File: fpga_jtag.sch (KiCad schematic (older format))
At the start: 2 parts

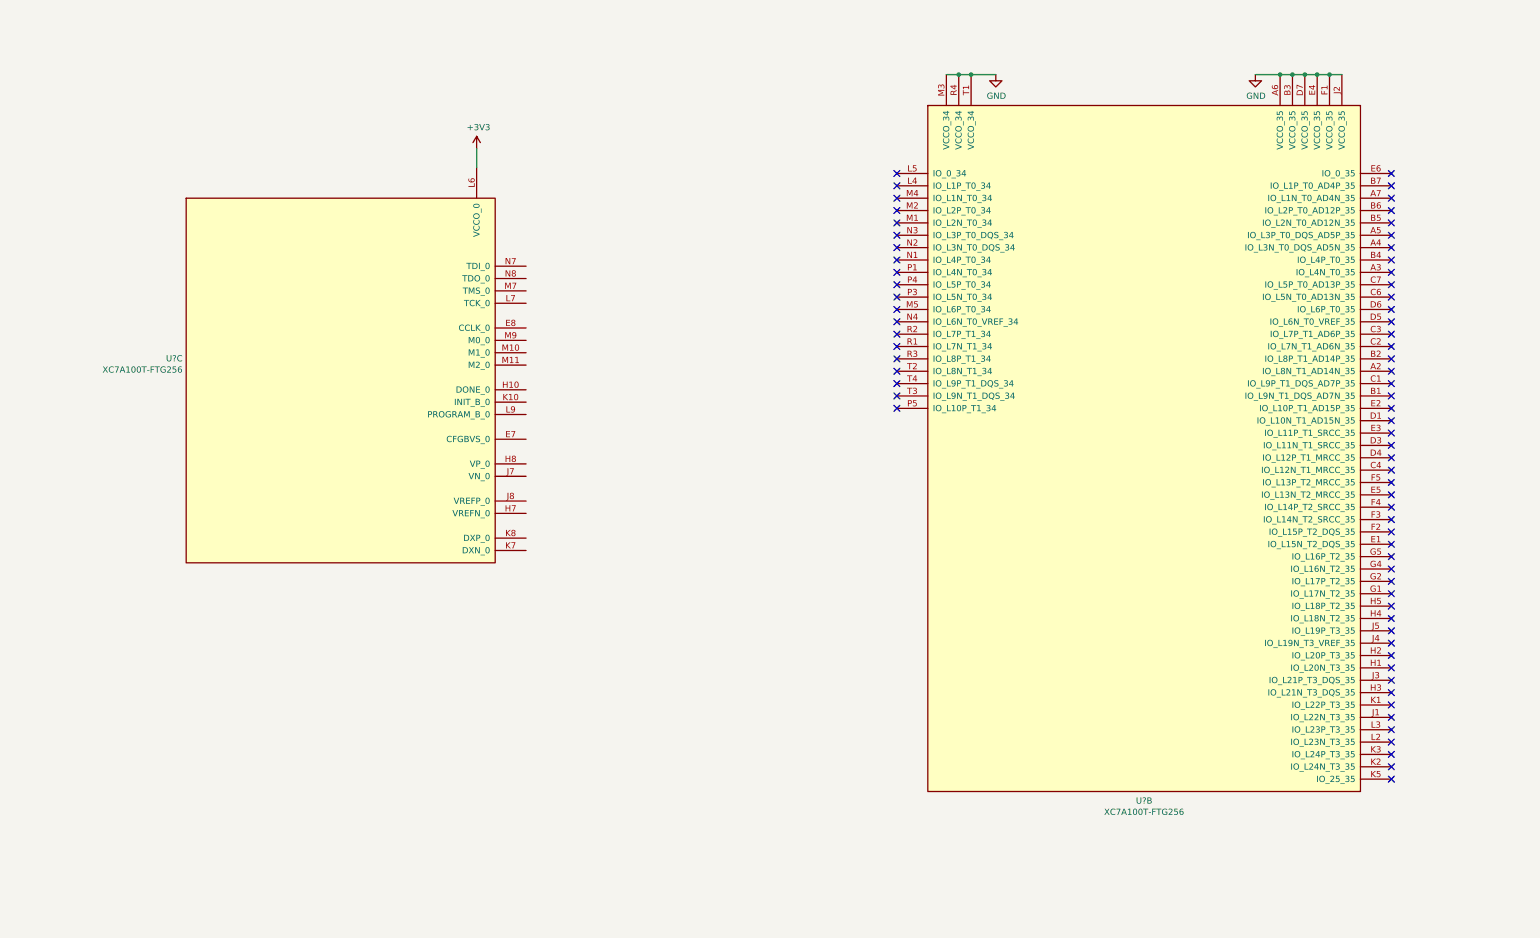
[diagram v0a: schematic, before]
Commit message: Add JTAG connector
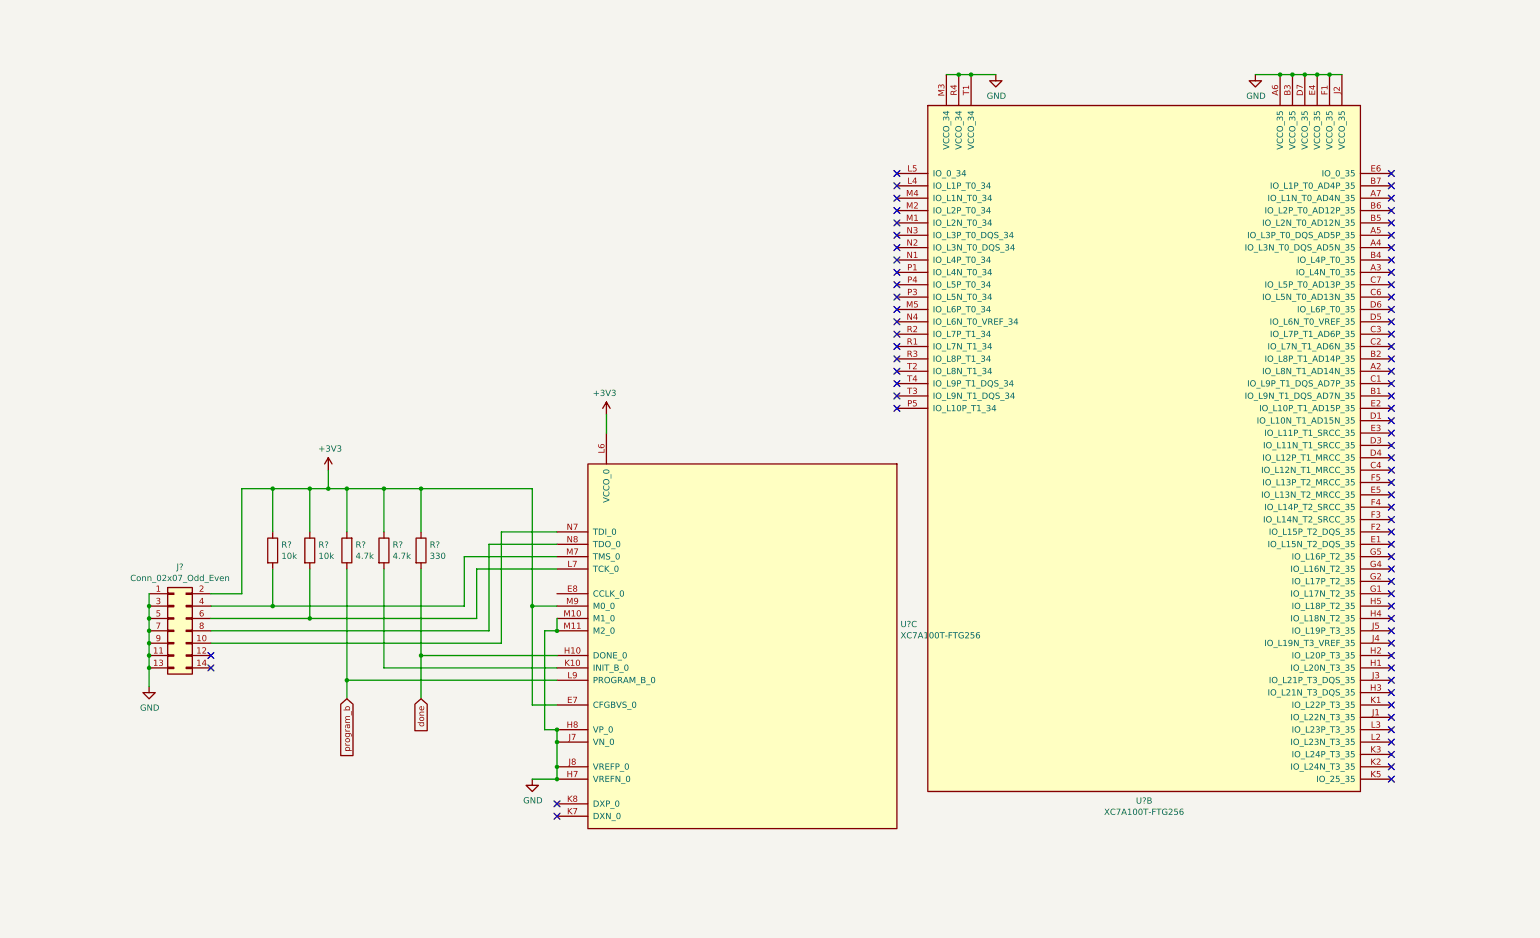
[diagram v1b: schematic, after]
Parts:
- added J?: Conn_02x07_Odd_Even, symbol Connector_Generic:Conn_02x07_Odd_Even
- added R? (x2): 10k, symbol Device:R
- added R? (x2): 4.7k, symbol Device:R
- added R?: 330, symbol Device:R
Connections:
- net +3V3: now also U?.E7 (CFGBVS_0), U?.M9 (M0_0), J?.2 (Pin_2), R?.1, R?.1, R?.1, R?.1, R?.2
- net GND: now also U?.H7 (VREFN_0), U?.H8 (VP_0), U?.J7 (VN_0), U?.J8 (VREFP_0), U?.M10 (M1_0), U?.M11 (M2_0), J?.1 (Pin_1), J?.11 (Pin_11), J?.13 (Pin_13), J?.3 (Pin_3), J?.5 (Pin_5), J?.7 (Pin_7), J?.9 (Pin_9)
- net done: now reaches U?.H10 (DONE_0)
- net done: now also R?.2
- net at U?.K10 (INIT_B_0): now also R?.2
- net at U?.L7 (TCK_0): now also J?.6 (Pin_6), R?.2
- net program_b: now reaches U?.L9 (PROGRAM_B_0)
- net program_b: now also R?.1
- net at U?.M7 (TMS_0): now also J?.4 (Pin_4), R?.2
- net at U?.N7 (TDI_0): now also J?.10 (Pin_10)
- net at U?.N8 (TDO_0): now also J?.8 (Pin_8)
- no-connect marks 70 -> 74
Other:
- moved on the sheet: U?C

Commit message: Switch FPGA I/O banks, and add subsheet for SRAM
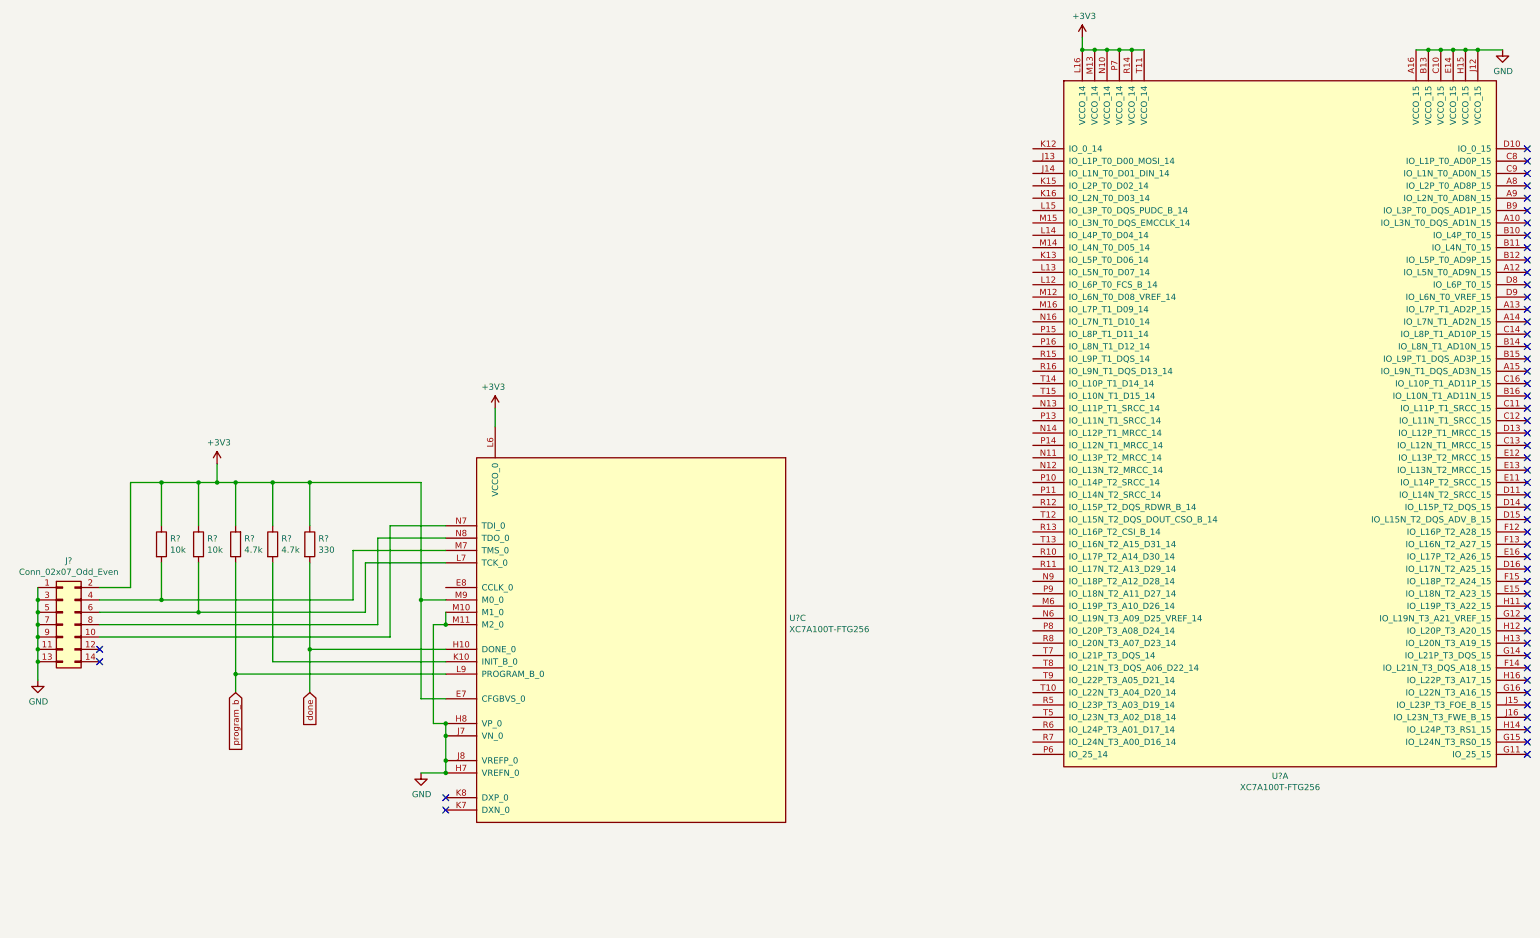
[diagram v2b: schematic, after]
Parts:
- removed U?: XC7A100T-FTG256, symbol FPGA_Xilinx_Artix7:XC7A100T-FTG256
- added U?: XC7A100T-FTG256, symbol FPGA_Xilinx_Artix7:XC7A100T-FTG256
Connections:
- net +3V3: now also U?.L16 (VCCO_14), U?.M13 (VCCO_14), U?.N10 (VCCO_14), U?.P7 (VCCO_14), U?.R14 (VCCO_14), U?.T11 (VCCO_14)
- net GND: now also U?.A16 (VCCO_15), U?.B13 (VCCO_15), U?.C10 (VCCO_15), U?.E14 (VCCO_15), U?.H15 (VCCO_15), U?.J12 (VCCO_15)
- no-connect marks 74 -> 54
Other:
- moved on the sheet: J?, R?, U?C

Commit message: Add FPGA Flash
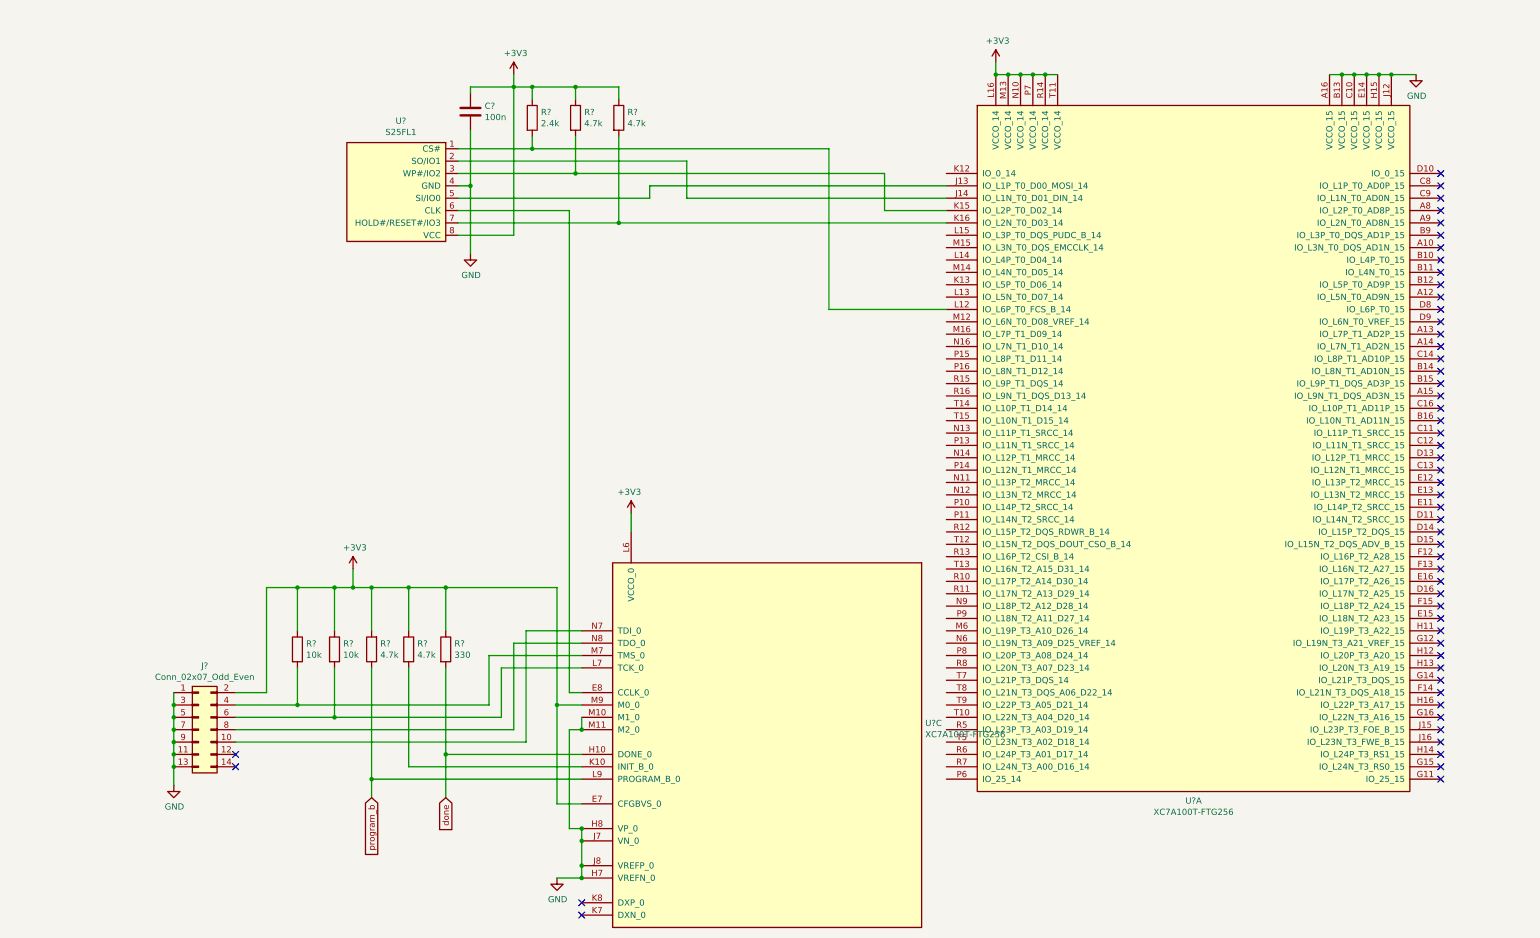
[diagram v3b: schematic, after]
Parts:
- added C?: 100n, symbol Device:C
- added R?: 2.4k, symbol Device:R
- added R? (x2): 4.7k, symbol Device:R
- added U?: S25FL1, symbol flash_memory:S25FL1
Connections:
- net +3V3: now also C?.1, R?.1, R?.1, R?.1, U?.8 (VCC)
- net GND: now also C?.2, U?.4 (GND)
- net at U?.E8 (CCLK_0): now also U?.6 (CLK)
- net at U?.J13 (IO_L1P_T0_D00_MOSI_14): now also U?.5 (SI/IO0)
- net at U?.J14 (IO_L1N_T0_D01_DIN_14): now also U?.2 (SO/IO1)
- net at U?.K15 (IO_L2P_T0_D02_14): now also R?.2, U?.3 (WP#/IO2)
- net at U?.K16 (IO_L2N_T0_D03_14): now also R?.2, U?.7 (HOLD#/RESET#/IO3)
- net at U?.L12 (IO_L6P_T0_FCS_B_14): now also R?.2, U?.1 (CS#)
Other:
- moved on the sheet: J?, R?, U?A, U?C
